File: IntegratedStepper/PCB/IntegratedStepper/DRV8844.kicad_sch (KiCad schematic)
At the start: 4 parts, among them IC1 DRV8844PWPR

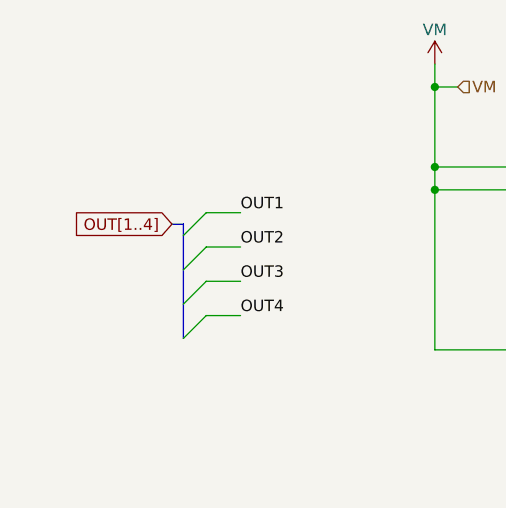
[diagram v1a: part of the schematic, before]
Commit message: update Vreg for Integrated Stepper
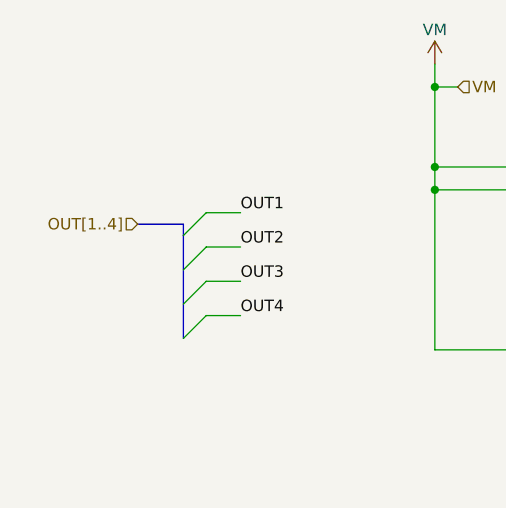
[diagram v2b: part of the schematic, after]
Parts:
- IC1: footprint SOP65P640X120-29N -> SamacSys_Parts:SOP65P640X120-29N
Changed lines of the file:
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@@
     (stroke (width 0) (type default))
   )
-  (bus (pts (xy 66.04 78.74) (xy 67.31 78.74))
+  (bus (pts (xy 62.23 78.74) (xy 67.31 78.74))
     (stroke (width 0) (type default))
   )
@@
     (stroke (width 0) (type default))
   )
-  (label "IN3" (at 219.71 78.74 0)
-    (effects (font (size 1.27 1.27)) (justify left bottom))
-  )
-  (label "OUT3" (at 73.66 85.09 0)
-    (effects (font (size 1.27 1.27)) (justify left bottom))
-  )
-  (label "IN4" (at 219.71 83.82 0)
+  (label "IN3" (at 219.71 78.74 0) (fields_autoplaced)
+    (effects (font (size 1.27 1.27)) (justify left bottom))
+  )
+  (label "OUT3" (at 73.66 85.09 0) (fields_autoplaced)
+    (effects (font (size 1.27 1.27)) (justify left bottom))
+  )
+  (label "IN4" (at 219.71 83.82 0) (fields_autoplaced)
     (effects (font (size 1.27 1.27)) (justify left bottom))
   )
@@
     (effects (font (size 1.27 1.27)) (justify left bottom))
   )
-  (label "OUT1" (at 73.66 77.47 0)
+  (label "OUT1" (at 73.66 77.47 0) (fields_autoplaced)
     (effects (font (size 1.27 1.27)) (justify left bottom))
   )
@@
     (effects (font (size 1.27 1.27)) (justify left bottom))
   )
-  (label "EN2" (at 175.26 77.47 0)
-    (effects (font (size 1.27 1.27)) (justify left bottom))
-  )
-  (label "OUT2" (at 73.66 81.28 0)
-    (effects (font (size 1.27 1.27)) (justify left bottom))
-  )
-  (label "OUT4" (at 73.66 88.9 0)
+  (label "EN2" (at 175.26 77.47 0) (fields_autoplaced)
+    (effects (font (size 1.27 1.27)) (justify left bottom))
+  )
+  (label "OUT2" (at 73.66 81.28 0) (fields_autoplaced)
+    (effects (font (size 1.27 1.27)) (justify left bottom))
+  )
+  (label "OUT4" (at 73.66 88.9 0) (fields_autoplaced)
     (effects (font (size 1.27 1.27)) (justify left bottom))
   )
@@
     (effects (font (size 1.27 1.27)) (justify left bottom))
   )
-  (label "EN4" (at 175.26 87.63 0)
-    (effects (font (size 1.27 1.27)) (justify left bottom))
-  )
-  (label "EN1" (at 175.26 72.39 0)
+  (label "EN4" (at 175.26 87.63 0) (fields_autoplaced)
+    (effects (font (size 1.27 1.27)) (justify left bottom))
+  )
+  (label "EN1" (at 175.26 72.39 0) (fields_autoplaced)
     (effects (font (size 1.27 1.27)) (justify left bottom))
   )
@@
     (effects (font (size 1.27 1.27)) (justify left bottom))
   )
-  (label "IN2" (at 219.71 73.66 0)
+  (label "IN2" (at 219.71 73.66 0) (fields_autoplaced)
     (effects (font (size 1.27 1.27)) (justify left bottom))
   )
@@
     (effects (font (size 1.27 1.27)) (justify left bottom))
   )
-  (label "EN3" (at 175.26 82.55 0)
-    (effects (font (size 1.27 1.27)) (justify left bottom))
-  )
-  (label "IN1" (at 219.71 68.58 0)
-    (effects (font (size 1.27 1.27)) (justify left bottom))
-  )
-  (global_label "OUT[1..4]" (shape input) (at 66.04 78.74 180) (fields_autoplaced)
+  (label "EN3" (at 175.26 82.55 0) (fields_autoplaced)
+    (effects (font (size 1.27 1.27)) (justify left bottom))
+  )
+  (label "IN1" (at 219.71 68.58 0) (fields_autoplaced)
+    (effects (font (size 1.27 1.27)) (justify left bottom))
+  )
+  (hierarchical_label "NFAULT" (shape input) (at 170.18 92.71 0) (fields_autoplaced)
+    (effects (font (size 1.27 1.27)) (justify left))
+  )
+  (hierarchical_label "VM" (shape input) (at 97.79 63.5 0) (fields_autoplaced)
+    (effects (font (size 1.27 1.27)) (justify left))
+  )
+  (hierarchical_label "NSLEEP" (shape input) (at 170.18 95.25 0) (fields_autoplaced)
+    (effects (font (size 1.27 1.27)) (justify left))
+  )
+  (hierarchical_label "EN[1..4]" (shape input) (at 205.74 62.23 0) (fields_autoplaced)
+    (effects (font (size 1.27 1.27)) (justify left))
+  )
+  (hierarchical_label "IN[1..4]" (shape input) (at 228.6 66.04 0) (fields_autoplaced)
+    (effects (font (size 1.27 1.27)) (justify left))
+  )
+  (hierarchical_label "NRESET" (shape input) (at 170.18 97.79 0) (fields_autoplaced)
+    (effects (font (size 1.27 1.27)) (justify left))
+  )
+  (hierarchical_label "VM-" (shape input) (at 113.03 100.33 180) (fields_autoplaced)
     (effects (font (size 1.27 1.27)) (justify right))
-    (property "Intersheetrefs" "${INTERSHEET_REFS}" (at 54.1836 78.74 0)
-      (effects (font (size 1.27 1.27)) (justify right) hide)
-    )
-  )
-  (hierarchical_label "NFAULT" (shape input) (at 170.18 92.71 0) (fields_autoplaced)
-    (effects (font (size 1.27 1.27)) (justify left))
-  )
-  (hierarchical_label "VM" (shape input) (at 97.79 63.5 0) (fields_autoplaced)
-    (effects (font (size 1.27 1.27)) (justify left))
-  )
-  (hierarchical_label "NSLEEP" (shape input) (at 170.18 95.25 0) (fields_autoplaced)
-    (effects (font (size 1.27 1.27)) (justify left))
-  )
-  (hierarchical_label "EN[1..4]" (shape input) (at 205.74 62.23 0) (fields_autoplaced)
-    (effects (font (size 1.27 1.27)) (justify left))
-  )
-  (hierarchical_label "IN[1..4]" (shape input) (at 228.6 66.04 0) (fields_autoplaced)
-    (effects (font (size 1.27 1.27)) (justify left))
-  )
-  (hierarchical_label "NRESET" (shape input) (at 170.18 97.79 0) (fields_autoplaced)
-    (effects (font (size 1.27 1.27)) (justify left))
-  )
-  (hierarchical_label "VM-" (shape input) (at 113.03 100.33 180) (fields_autoplaced)
+  )
+  (hierarchical_label "OUT[1..4]" (shape input) (at 62.23 78.74 180) (fields_autoplaced)
     (effects (font (size 1.27 1.27)) (justify right))
   )
@@
       (effects (font (size 1.27 1.27)))
     )
-    (property "Footprint" "SOP65P640X120-29N" (at 163.83 64.77 0)
+    (property "Footprint" "SamacSys_Parts:SOP65P640X120-29N" (at 163.83 64.77 0)
       (effects (font (size 1.27 1.27)) (justify left) hide)
     )

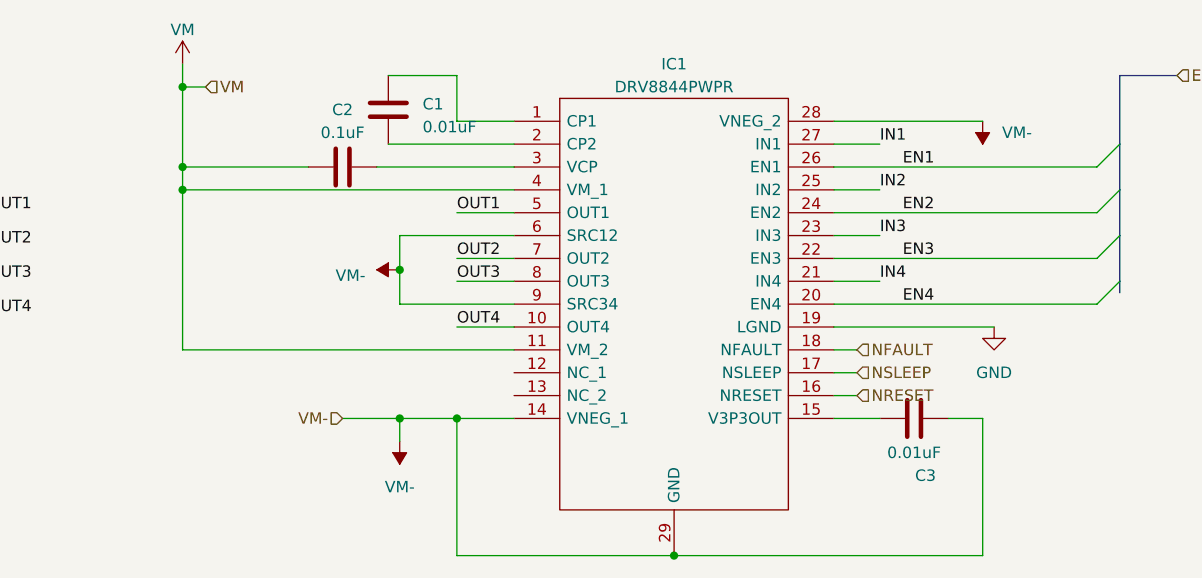
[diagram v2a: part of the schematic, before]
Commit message: Update Integrated Stepper PCB with ESP sch and CAN sch
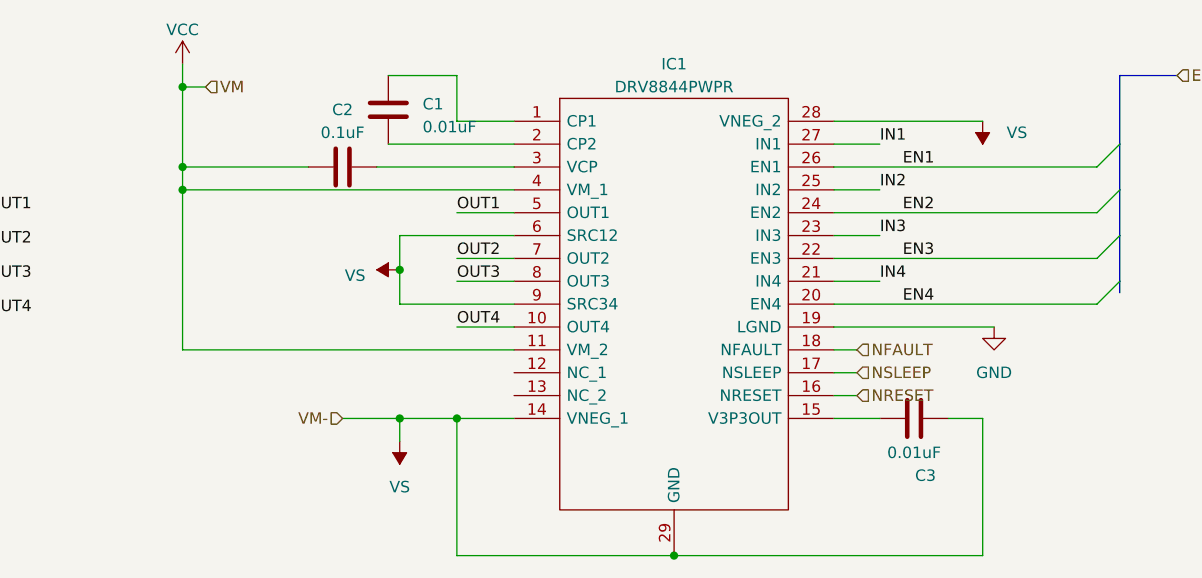
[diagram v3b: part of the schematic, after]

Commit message: Update Integrated Stepper with inital PCB
This is going to be so hard :(
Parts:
- added C22, C23, C28, C29: 22uF, Capacitor_SMD:C_0603_1608Metric, symbol Device:C
- added C24, C25, C26, C27, C30, C31, C32, C33: 10uF, Capacitor_SMD:C_0603_1608Metric, symbol Device:C
- added R19, R20: 2k, Resistor_SMD:R_0603_1608Metric, symbol Device:R_US
- added R21: 10K, Resistor_SMD:R_0603_1608Metric, symbol Device:R_US
- added VM1: LED, LED_SMD:LED_0603_1608Metric, symbol Device:LED
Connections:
- net NRESET: now also R19.2
- net NSLEEP: now also R20.2
- net VCC: now also C22.1, C23.1, C24.1, C25.1, C26.1, C27.1, C28.1, C29.1, C30.1, C31.1, C32.1, C33.1, VM1.2 (A)
- net VS: now also C22.2, C23.2, C24.2, C25.2, C26.2, C27.2, C28.2, C29.2, C30.2, C31.2, C32.2, C33.2, R21.1
- new net: R21.2, VM1.1 (K)
- new net 3V3_VCC: R19.1, R20.1

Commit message: add changes for instock parts
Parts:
- IC1: LCSC (none) -> C177807; LCSC Part (none) -> C177807; LCSC Part Number (none) -> C177807
- R19, R20: LCSC (none) -> C217936; LCSC Part (none) -> C217936; LCSC Part Number (none) -> C217936
- R21: LCSC (none) -> C469659; LCSC Part (none) -> C469659; LCSC Part Number (none) -> C469659
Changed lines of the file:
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@@
+			)
+		)
+		(property "LCSC" " C177807"
+			(at 132.08 67.31 0)
+			(effects
+				(font
+					(size 1.27 1.27)
+				)
+				(hide yes)
+			)
+		)
+		(property "LCSC Part" " C177807"
+			(at 132.08 67.31 0)
+			(effects
+				(font
+					(size 1.27 1.27)
+				)
+				(hide yes)
+			)
+		)
+		(property "LCSC Part Number" " C177807"
+			(at 132.08 67.31 0)
+			(effects
+				(font
+					(size 1.27 1.27)
+				)
+				(hide yes)
 			)
 		)
@@
 			)
 		)
+		(property "LCSC" "C217936"
+			(at 219.71 99.06 0)
+			(effects
+				(font
+					(size 1.27 1.27)
+				)
+				(hide yes)
+			)
+		)
+		(property "LCSC Part" "C217936"
+			(at 219.71 99.06 0)
+			(effects
+				(font
+					(size 1.27 1.27)
+				)
+				(hide yes)
+			)
+		)
+		(property "LCSC Part Number" "C217936"
+			(at 219.71 99.06 0)
+			(effects
+				(font
+					(size 1.27 1.27)
+				)
+				(hide yes)
+			)
+		)
 		(pin "2"
 		)
@@
 			)
 		)
+		(property "LCSC" "C469659"
+			(at 68.58 116.84 0)
+			(effects
+				(font
+					(size 1.27 1.27)
+				)
+				(hide yes)
+			)
+		)
+		(property "LCSC Part" "C469659"
+			(at 68.58 116.84 0)
+			(effects
+				(font
+					(size 1.27 1.27)
+				)
+				(hide yes)
+			)
+		)
+		(property "LCSC Part Number" "C469659"
+			(at 68.58 116.84 0)
+			(effects
+				(font
+					(size 1.27 1.27)
+				)
+				(hide yes)
+			)
+		)
 		(pin "2"
 		)
@@
 			(at 203.2 101.6 0)
 			(effects
+				(font
+					(size 1.27 1.27)
+				)
+				(hide yes)
+			)
+		)
+		(property "LCSC" "C217936"
+			(at 203.2 101.6 0)
+			(effects
+				(font
+					(size 1.27 1.27)
+				)
+				(hide yes)
+			)
+		)
+		(property "LCSC Part" "C217936"
+			(at 203.2 101.6 0)
+			(effects
+				(font
+					(size 1.27 1.27)
+				)
+				(hide yes)
+			)
+		)
+		(property "LCSC Part Number" "C217936"
+			(at 203.2 101.6 0)
+			(effects

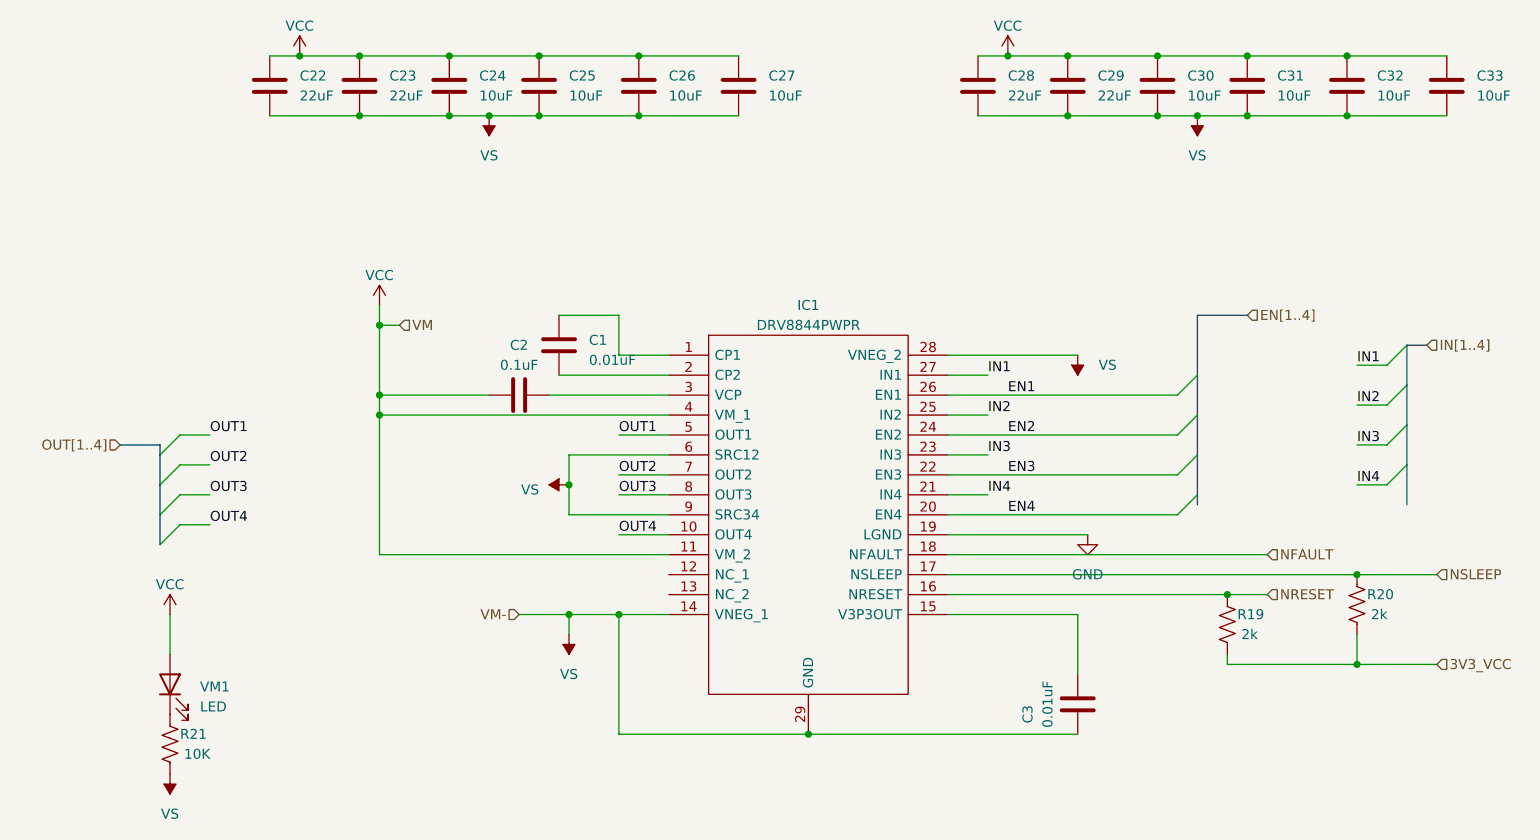
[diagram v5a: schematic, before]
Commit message: update with more in stock parts
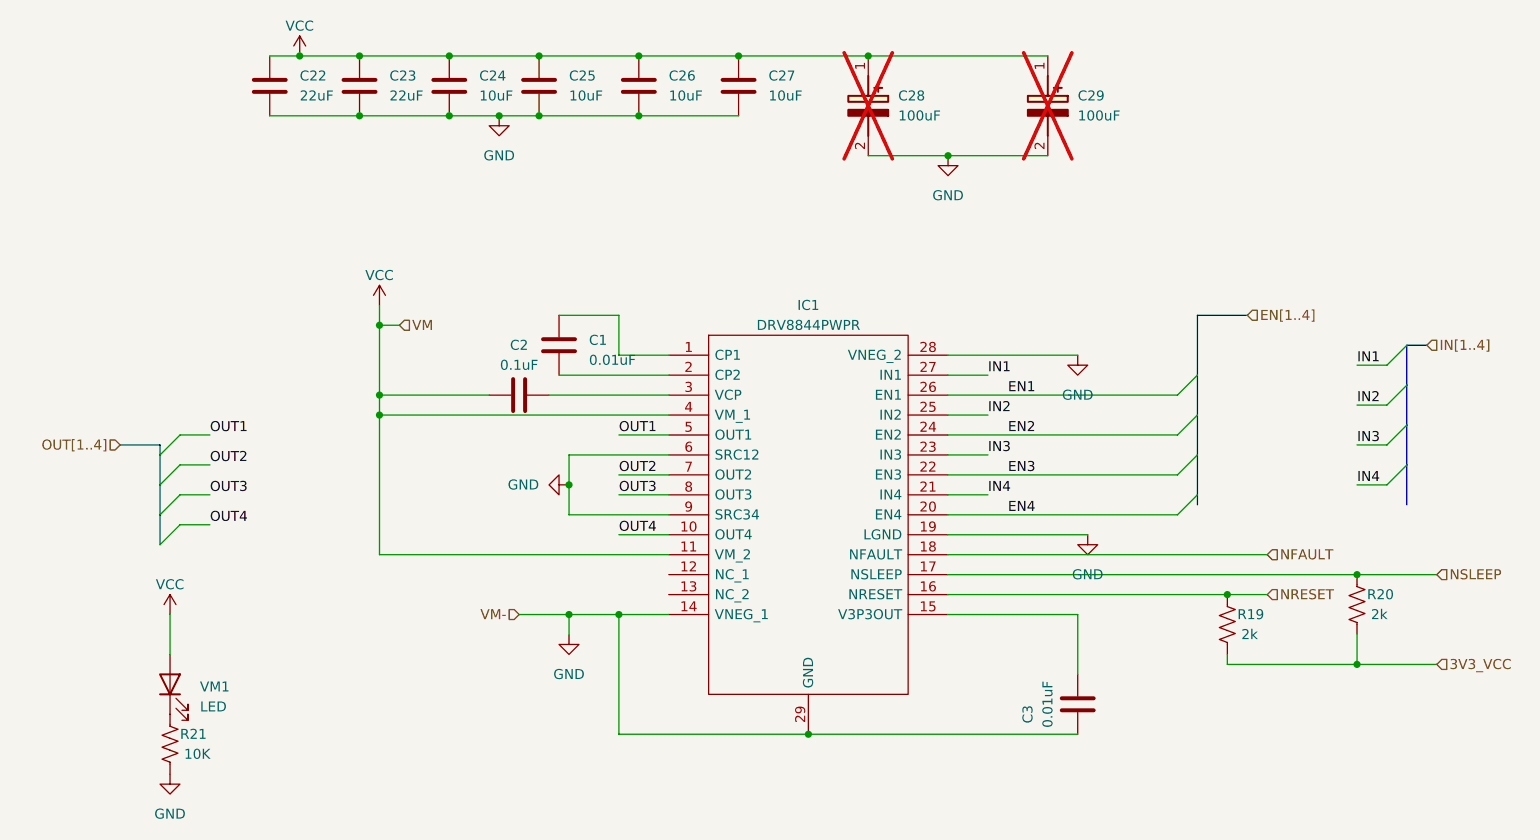
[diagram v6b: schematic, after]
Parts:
- removed C28, C29: 22uF, Capacitor_SMD:C_0603_1608Metric, symbol Device:C
- removed C30, C31, C32, C33: 10uF, Capacitor_SMD:C_0603_1608Metric, symbol Device:C
- added C28, C29: 100uF, CAPPRD350W65D800H1650, symbol SamacSys_Parts:EEU-FC1J101LB
- C1, C3: footprint Capacitor_SMD:C_0603_1608Metric_Pad1.08x0.95mm_HandSolder -> Capacitor_SMD:C_0805_2012Metric; LCSC (none) -> C303894; LCSC Part (none) -> C303894; LCSC Part Number (none) -> C303894
- C2: footprint Capacitor_SMD:C_0603_1608Metric_Pad1.08x0.95mm_HandSolder -> Capacitor_SMD:C_0805_2012Metric; LCSC (none) -> C597290; LCSC Part (none) -> C597290; LCSC Part Number (none) -> C597290
- C22, C23: footprint Capacitor_SMD:C_0603_1608Metric -> Capacitor_SMD:C_1210_3225Metric; LCSC (none) -> C2929200; LCSC Part Number (none) -> C2929200; Voltage Rating (none) -> 100V
- C24, C26, C27: footprint Capacitor_SMD:C_0603_1608Metric -> Capacitor_SMD:C_1210_3225Metric; LCSC (none) -> C2929200; LCSC Part (none) -> C2929200; LCSC Part Number (none) -> C2929200
- C25: LCSC (none) -> C96446; LCSC Part (none) -> C96446; LCSC Part Number (none) -> C96446
- VM1: LCSC (none) -> C965804; LCSC Part (none) -> C965804; LCSC Part Number (none) -> C965804
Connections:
- net VS is gone; now on net GND: C22.2, C23.2, C24.2, C25.2, C26.2, C27.2, C3.1, IC1.14 (VNEG_1), IC1.28 (VNEG_2), IC1.29 (GND), IC1.6 (SRC12), IC1.9 (SRC34), R21.1
- net GND: now also C28.2 (-), C29.2 (-)
- net VCC: now also C28.1 (+), C29.1 (+)
